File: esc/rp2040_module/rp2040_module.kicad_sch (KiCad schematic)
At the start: 29 parts, among them J1 USB_C_Receptacle_USB2.0, J2 Conn_01x04, SW10 SW_Push, SW11 SW_Push, U1 RP2040, U3 W25Q64JVXGIQ, Y1 12MHz

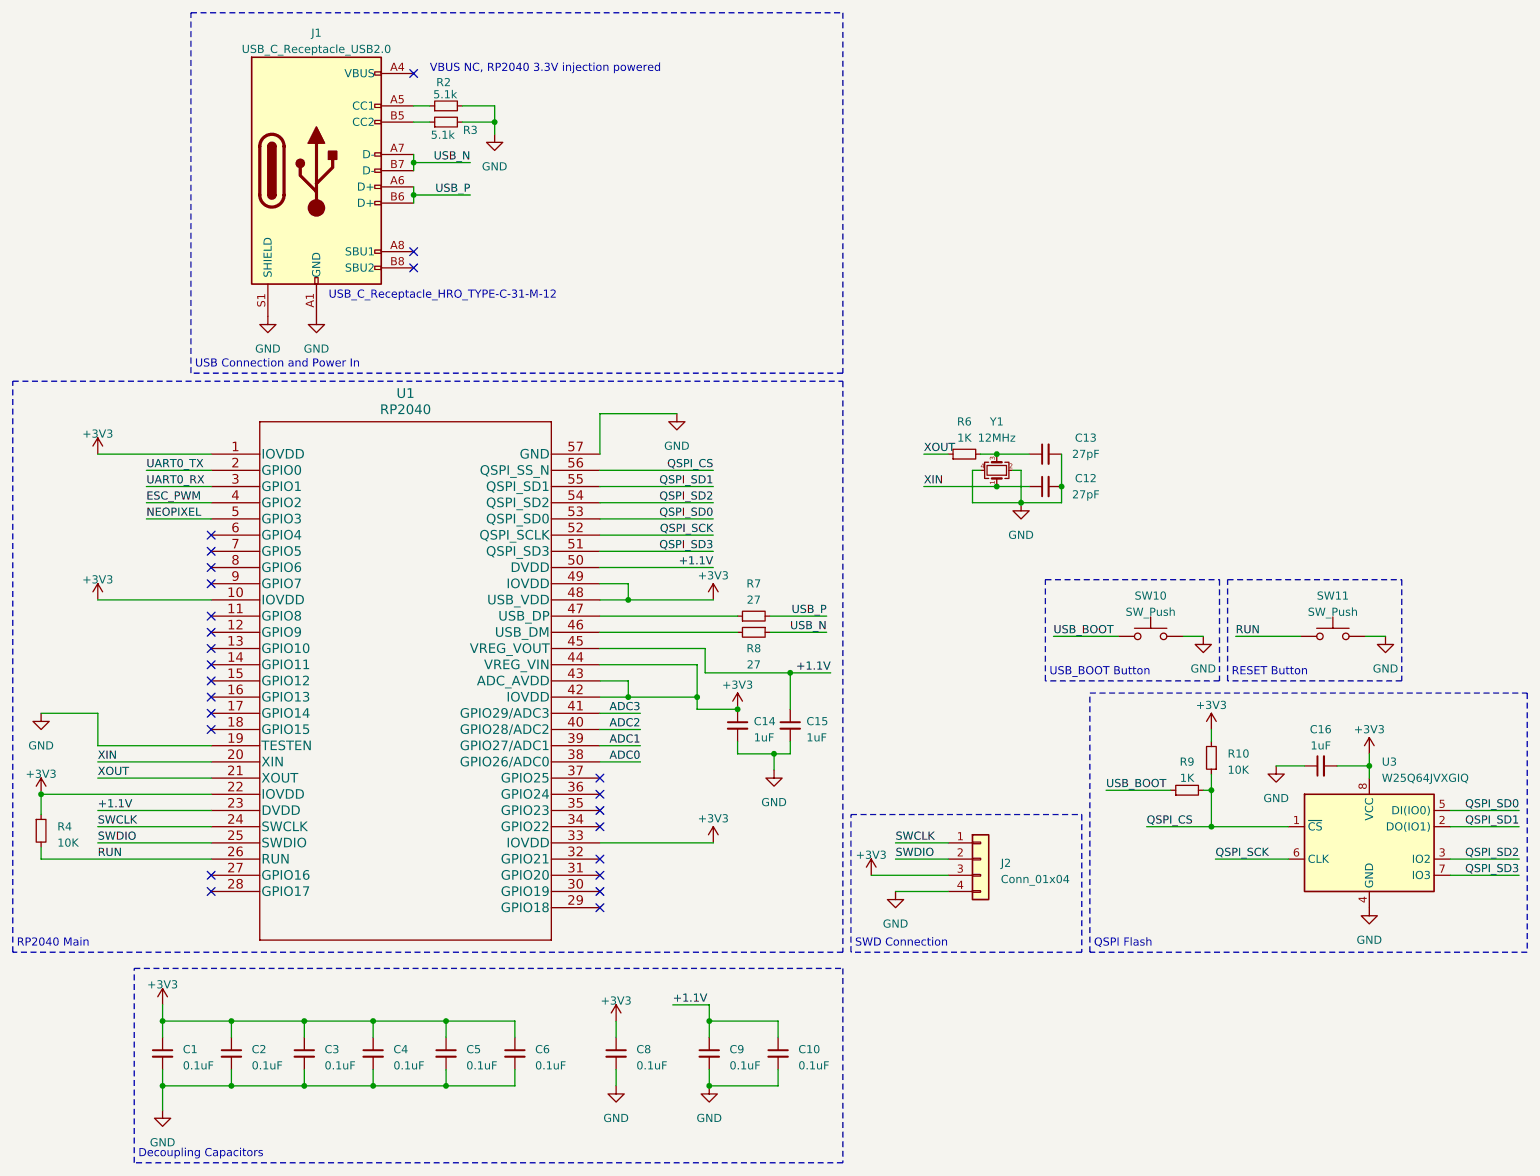
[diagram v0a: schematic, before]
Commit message: Feat[esc]: schematic to pcb placement of B-G431B-ESC1 + RP2040
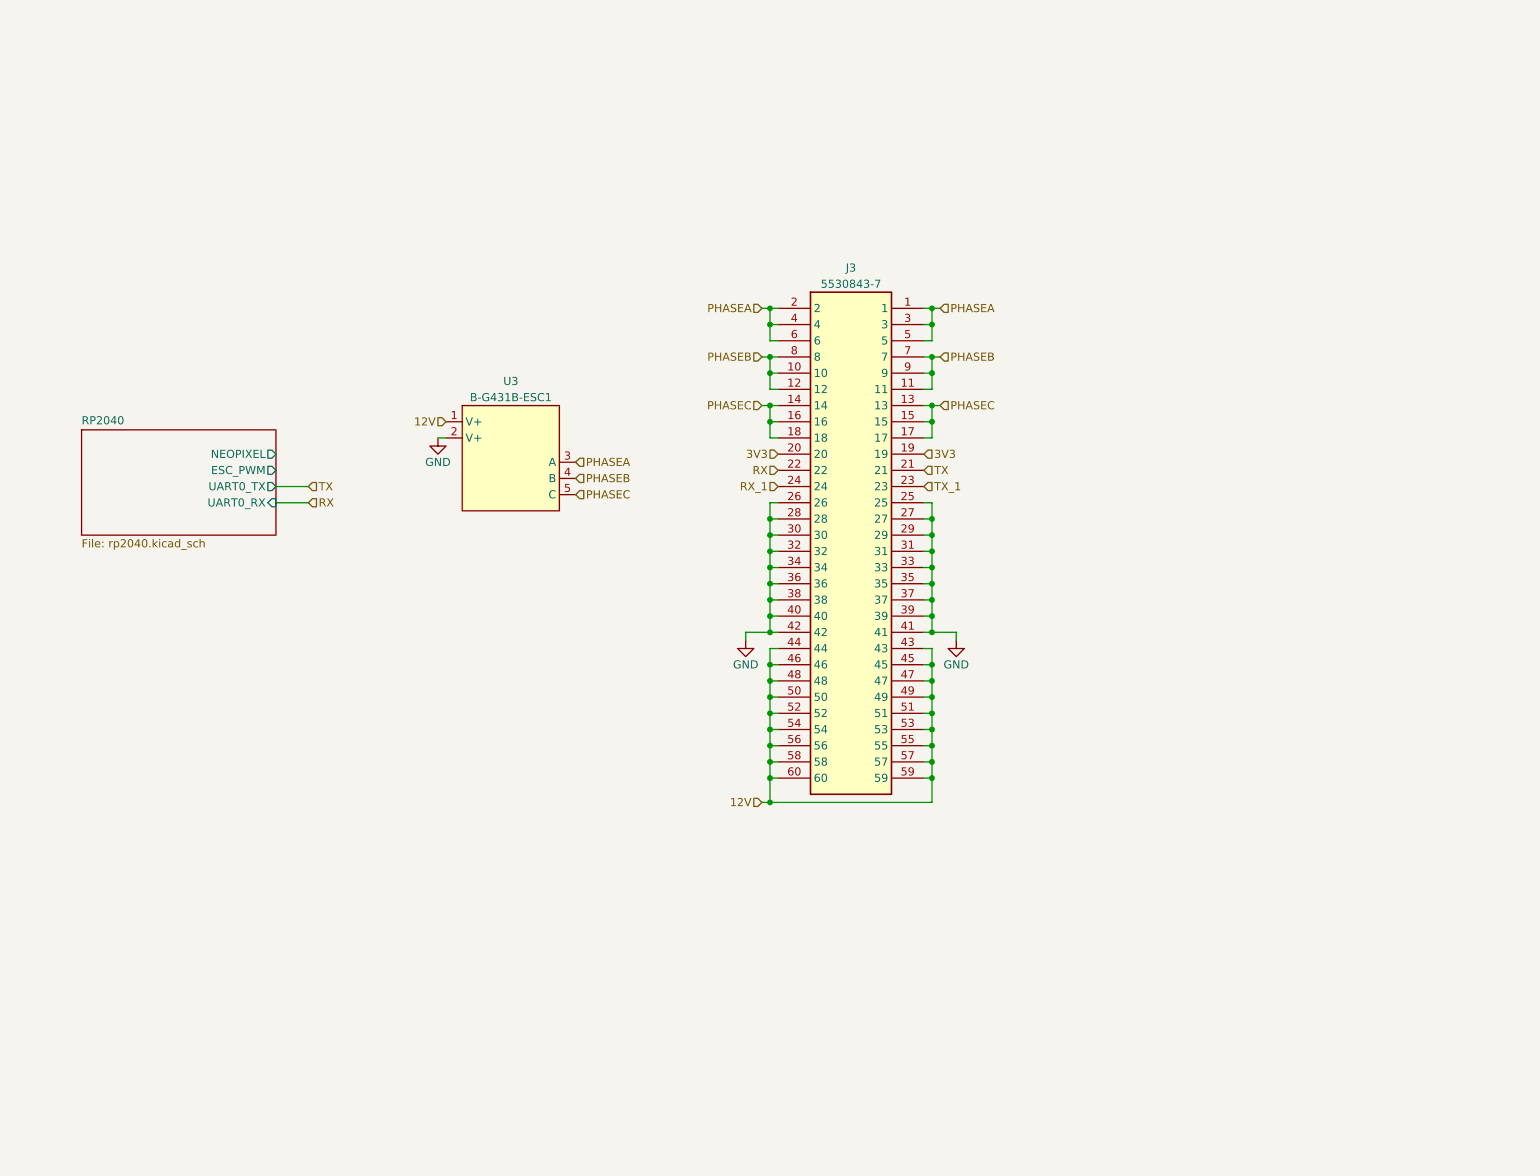
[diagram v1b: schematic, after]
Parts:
- removed C1, C10, C2, C3, C4, C5, C6, C8, C9: 0.1uF, Capacitor_SMD:C_0402_1005Metric, symbol Device:C_Small
- removed C12, C13: 27pF, Capacitor_SMD:C_0402_1005Metric, symbol Device:C_Small
- removed C14, C15, C16: 1uF, Capacitor_SMD:C_0402_1005Metric, symbol Device:C_Small
- removed J1: USB_C_Receptacle_USB2.0, Connector_USB:USB_C_Receptacle_HRO_TYPE-C-31-M-12, symbol Connector:USB_C_Receptacle_USB2.0
- removed J2: Conn_01x04, Connector_PinHeader_2.54mm:PinHeader_1x04_P2.54mm_Vertical, symbol Connector_Generic:Conn_01x04
- removed R10, R4: 10K, Resistor_SMD:R_0402_1005Metric, symbol Device:R_Small
- removed R2, R3: 5.1k, Resistor_SMD:R_0402_1005Metric, symbol Device:R_Small
- removed R6, R9: 1K, Resistor_SMD:R_0402_1005Metric, symbol Device:R_Small
- removed R7, R8: 27, Resistor_SMD:R_0603_1608Metric, symbol Device:R_Small
- removed SW10, SW11: SW_Push, SLIM_6MM_SWITCH:SW_PUSH_6mm_SLIM, symbol Switch:SW_Push
- removed U1: RP2040, Package_DFN_QFN:QFN-56-1EP_7x7mm_P0.4mm_EP3.2x3.2mm_ThermalVias, symbol 2022-10-24_20-36-00:RP2040
- removed U3: W25Q64JVXGIQ, W25Q64JVXGIQ:DFN_XGIQ TR_WIN-M, symbol Memory_Flash:W25Q32JVSS
- removed Y1: 12MHz, Crystal:Crystal_SMD_2016-4Pin_2.0x1.6mm, symbol Device:Crystal_GND24_Small
- added J3: 5530843-7, 5530843-7_PCB_Edge:TE_5530843-7_PCB_Edge, symbol Card_Edge:5530843-7
- added U3: B-G431B-ESC1, B-G431B-ESC1:B-G431B-ESC1_MOUNT, symbol B-G431B-ESC1:B-G431B-ESC1
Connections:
- net GND: now also J3.25, J3.26, J3.27, J3.28, J3.29, J3.30, J3.31, J3.32, J3.33, J3.34, J3.35, J3.36, J3.37, J3.38, J3.39, J3.40, J3.41, J3.42, U3.2 (V+)
- new net 12V: J3.43, J3.44, J3.45, J3.46, J3.47, J3.48, J3.49, J3.50, J3.51, J3.52, J3.53, J3.54, J3.55, J3.56, J3.57, J3.58, J3.59, J3.60, U3.1 (V+)
- new net 3V3: J3.19, J3.20
- new net PHASEA: J3.1, J3.2, J3.3, J3.4, J3.5, J3.6, U3.3 (A)
- new net PHASEB: J3.10, J3.11, J3.12, J3.7, J3.8, J3.9, U3.4 (B)
- new net PHASEC: J3.13, J3.14, J3.15, J3.16, J3.17, J3.18, U3.5 (C)
- new net RX: J3.22
- new net RX_1: J3.24
- new net TX: J3.21
- new net TX_1: J3.23
- no-connect marks 25 -> 0
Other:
- added sheet RP2040 (rp2040.kicad_sch)
- note removed: "Decoupling Capacitors"
- note removed: "QSPI Flash"
- note removed: "RESET Button"
- note removed: "RP2040 Main"
- note removed: "SWD Connection"
- note removed: "USB Connection and Power In"
- note removed: "USB_BOOT Button"
- note removed: "USB_C_Receptacle_HRO_TYPE-C-31-M-12"
- note removed: "VBUS NC, RP2040 3.3V injection powered"
